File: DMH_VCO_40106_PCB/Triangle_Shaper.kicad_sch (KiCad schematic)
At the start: 15 parts, among them Q3 BC548, Q4 BC548, U3 TL072

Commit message: Added Cermet 3296W fp to trimpots
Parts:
- RV8: footprint (none) -> Potentiometer_THT:Potentiometer_Bourns_3296W_Vertical
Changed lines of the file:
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@@
 			)
 		)
-		(property "Footprint" ""
+		(property "Footprint" "Potentiometer_THT:Potentiometer_Bourns_3296W_Vertical"
 			(at 121.92 83.82 0)
 			(effects

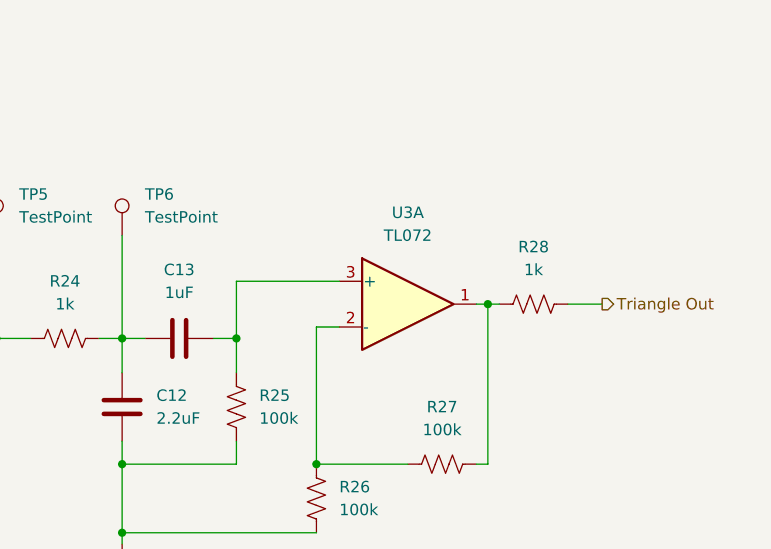
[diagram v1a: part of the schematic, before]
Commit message: Made U3 into TL074 instead of TL072
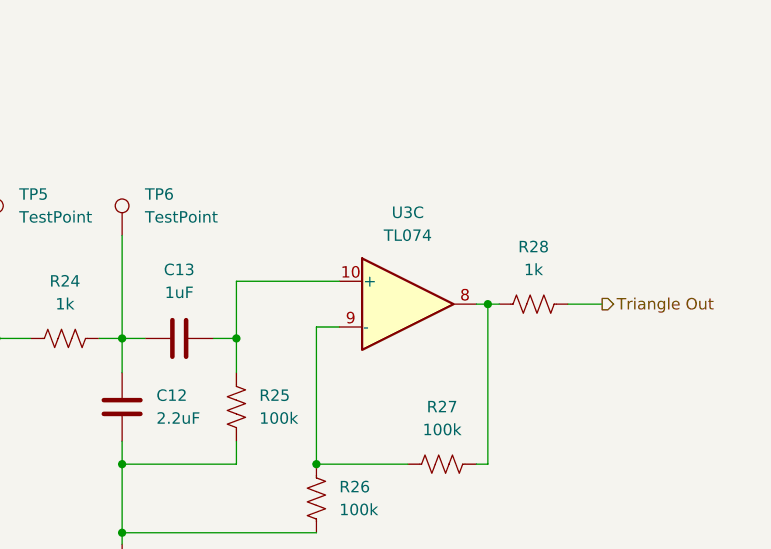
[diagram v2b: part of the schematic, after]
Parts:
- removed U3: TL072, symbol Amplifier_Operational:TL072
- added U3: TL074, symbol Amplifier_Operational:TL074
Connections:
- net at R26.1, R27.1: now also U3.9 (-)
- net at R27.2, R28.1: now also U3.8
- net at C13.2, R25.1: now also U3.10 (+)
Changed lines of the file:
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@@
+	)
+	(symbol
+		(lib_id "Amplifier_Operational:TL074")
+		(at 181.61 96.52 0)
+		(unit 3)
+		(exclude_from_sim no)
+		(in_bom yes)
+		(on_board yes)
+		(dnp no)
+		(fields_autoplaced yes)
+		(property "Reference" "U3"
+			(at 181.61 86.36 0)
+			(effects
+				(font
+					(size 1.27 1.27)
+				)
+			)
+		)
+		(property "Value" "TL074"
+			(at 181.61 88.9 0)
+			(effects
+				(font
+					(size 1.27 1.27)
+				)
+			)
+		)
+		(property "Footprint" ""
+			(at 180.34 93.98 0)
+			(effects
+				(font
+					(size 1.27 1.27)
+				)
+				(hide yes)
+			)
+		)
+		(property "Datasheet" "http://www.ti.com/lit/ds/symlink/tl071.pdf"
+			(at 182.88 91.44 0)
+			(effects
+				(font
+					(size 1.27 1.27)
+				)
+				(hide yes)
+			)
+		)
+		(property "Description" "Quad Low-Noise JFET-Input Operational Amplifiers, DIP-14/SOIC-14"
+			(at 181.61 96.52 0)
+			(effects
+				(font
+					(size 1.27 1.27)
+				)
+				(hide yes)
+			)
+		)
+		(pin "5"
+		)
+		(pin "1"
+		)
+		(pin "8"
+		)
+		(pin "13"
+		)
+		(pin "6"
+		)
+		(pin "14"
+		)
+		(pin "10"
+		)
+		(pin "9"
+		)
+		(pin "11"
+		)
+		(pin "3"
+		)
+		(pin "7"
+		)
+		(pin "12"
+		)
+		(pin "2"
+		)
+		(pin "4"
+		)
+		(instances
+			(project ""
+				(path "/fefed352-c100-4617-bbfb-c55e7427b122/0e77ed5b-450a-412c-a492-589f053c9c73"
+					(reference "U3")
+					(unit 3)
+				)
+			)
+		)
 	)
 	(symbol
@@
 					(unit 1)
 				)
-			)
-		)
-	)
-	(symbol
-		(lib_id "Amplifier_Operational:TL072")
-		(at 181.61 96.52 0)
-		(unit 1)
-		(exclude_from_sim no)
-		(in_bom yes)
-		(on_board yes)
-		(dnp no)
-		(fields_autoplaced yes)
-		(property "Reference" "U3"
-			(at 181.61 86.36 0)
-			(effects
-				(font
-					(size 1.27 1.27)
-				)
-			)
-		)
-		(property "Value" "TL072"
-			(at 181.61 88.9 0)
-			(effects
-				(font
-					(size 1.27 1.27)
-				)
-			)
-		)
-		(property "Footprint" ""
-			(at 181.61 96.52 0)
-			(effects
-				(font
-					(size 1.27 1.27)
-				)
-				(hide yes)
-			)
-		)
-		(property "Datasheet" "http://www.ti.com/lit/ds/symlink/tl071.pdf"
-			(at 181.61 96.52 0)
-			(effects
-				(font
-					(size 1.27 1.27)
-				)
-				(hide yes)
-			)
-		)
-		(property "Description" "Dual Low-Noise JFET-Input Operational Amplifiers, DIP-8/SOIC-8"
-			(at 181.61 96.52 0)
-			(effects
-				(font
-					(size 1.27 1.27)
-				)
-				(hide yes)
-			)
-		)
-		(pin "5"
-		)
-		(pin "1"
-		)
-		(pin "8"
-		)
-		(pin "7"
-		)
-		(pin "2"
-		)
-		(pin "4"
-		)
-		(pin "3"
-		)
-		(pin "6"
-		)
-		(instances
-			(project ""
-				(path "/fefed352-c100-4617-bbfb-c55e7427b122/0e77ed5b-450a-412c-a492-589f053c9c73"
-					(reference "U3")
-					(unit 1)
-				)

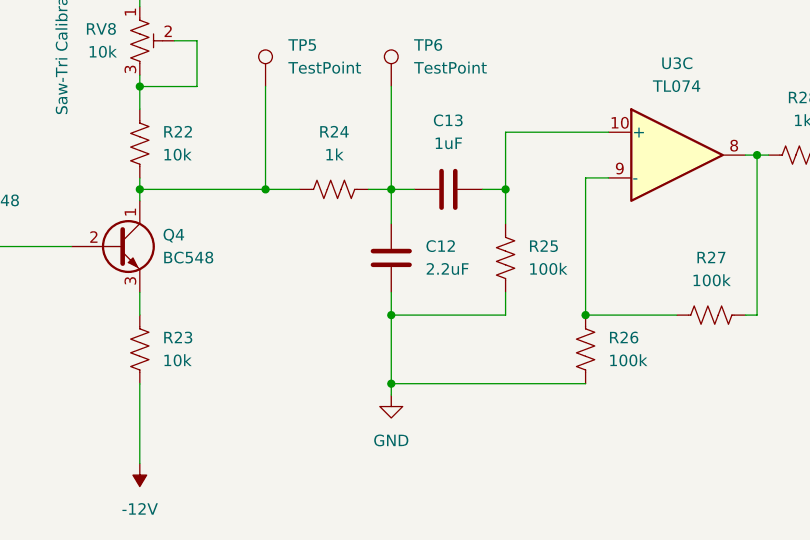
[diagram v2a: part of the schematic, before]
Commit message: Added not about 2.2uF cap
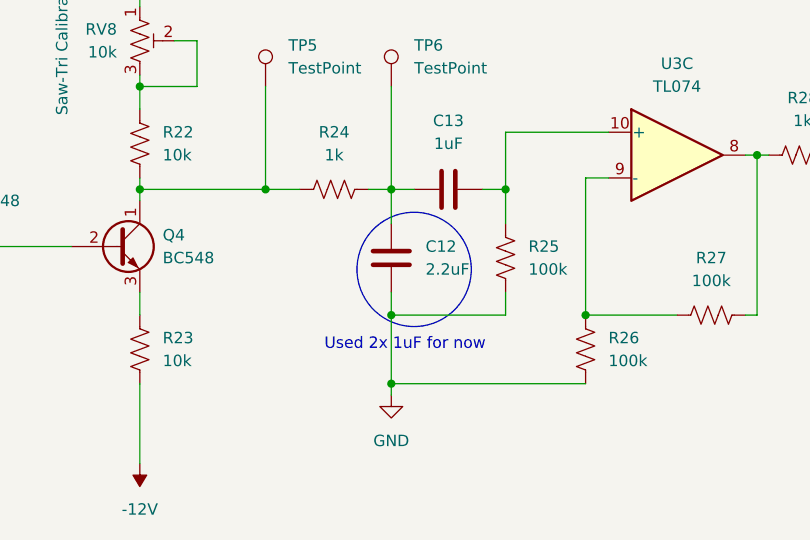
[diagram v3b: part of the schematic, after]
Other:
- note added: "Used 2x 1uF for now"
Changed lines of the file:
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@@
+		)
+	)
+	(circle
+		(center 152.4 109.22)
+		(radius 6.35)
+		(stroke
+			(width 0)
+			(type default)
+		)
+		(fill
+			(type none)
+		)
+	)
+	(text "Used 2x 1uF for now"
+		(exclude_from_sim no)
+		(at 151.384 117.602 0)
+		(effects
+			(font
+				(size 1.27 1.27)
+			)
 		)
 	)

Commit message: Corrected capacitor value
Should be 2.2nF, not 2.2uF
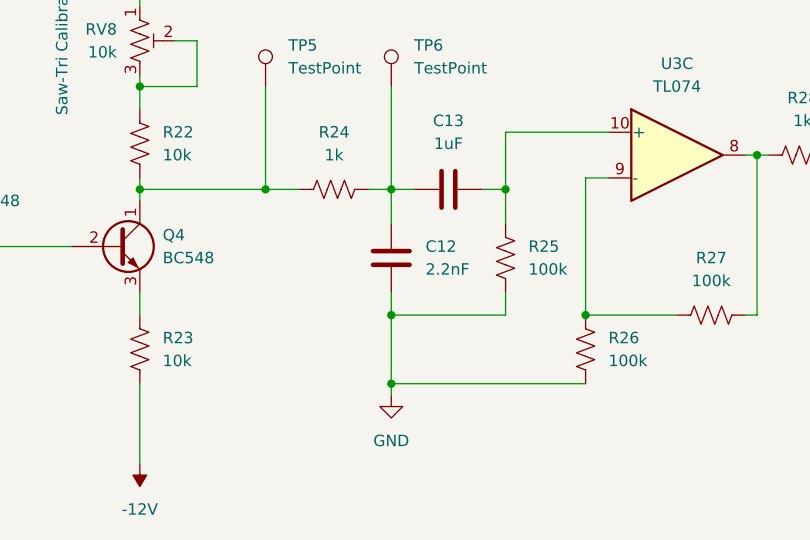
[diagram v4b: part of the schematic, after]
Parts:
- C12: value 2.2uF -> 2.2nF
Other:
- note removed: "Used 2x 1uF for now"
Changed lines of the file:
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@@
-		)
-	)
-	(circle
-		(center 152.4 109.22)
-		(radius 6.35)
-		(stroke
-			(width 0)
-			(type default)
-		)
-		(fill
-			(type none)
-		)
-	)
-	(text "Used 2x 1uF for now"
-		(exclude_from_sim no)
-		(at 151.384 117.602 0)
-		(effects
-			(font
-				(size 1.27 1.27)
-			)
 		)
 	)
@@
 			)
 		)
-		(property "Value" "2.2uF"
+		(property "Value" "2.2nF"
 			(at 153.67 109.2199 0)
 			(effects

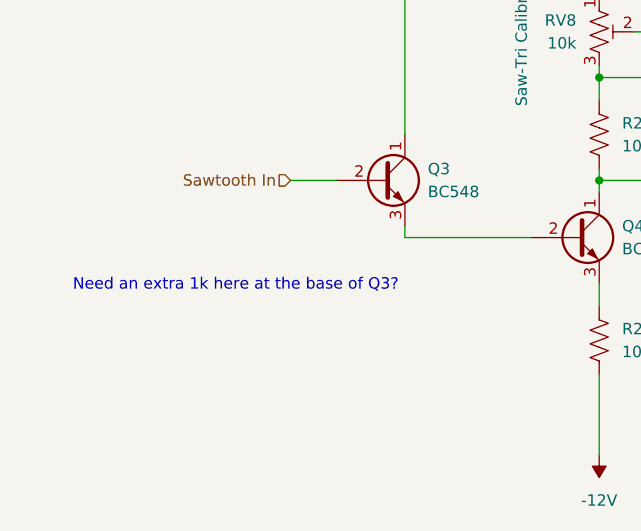
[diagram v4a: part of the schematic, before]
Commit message: Improved range of Coarse knob
... and allowed Centering knob to set C1=32,7Hz as root note with Coarse knob all the way CCW.
... and added 1kHz to Sine output.
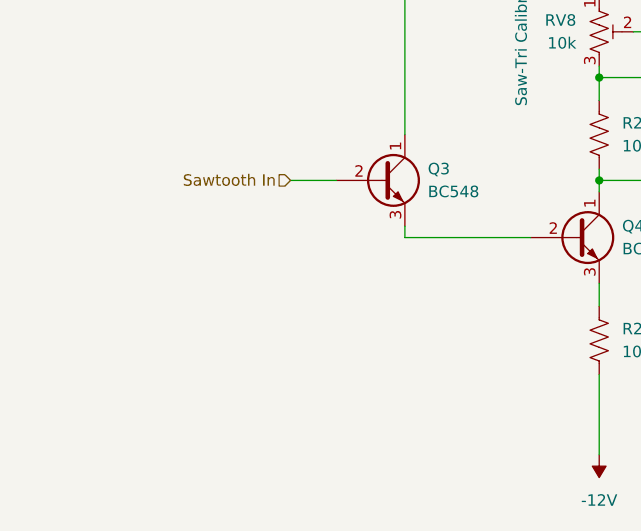
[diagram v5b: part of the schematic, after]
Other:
- note removed: "Need an extra 1k here at the base of Q3?"
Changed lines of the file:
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@@
-		)
-	)
-	(text "Need an extra 1k here at the base of Q3?"
-		(exclude_from_sim no)
-		(at 81.534 112.014 0)
-		(effects
-			(font
-				(size 1.27 1.27)
-			)
 		)
 	)

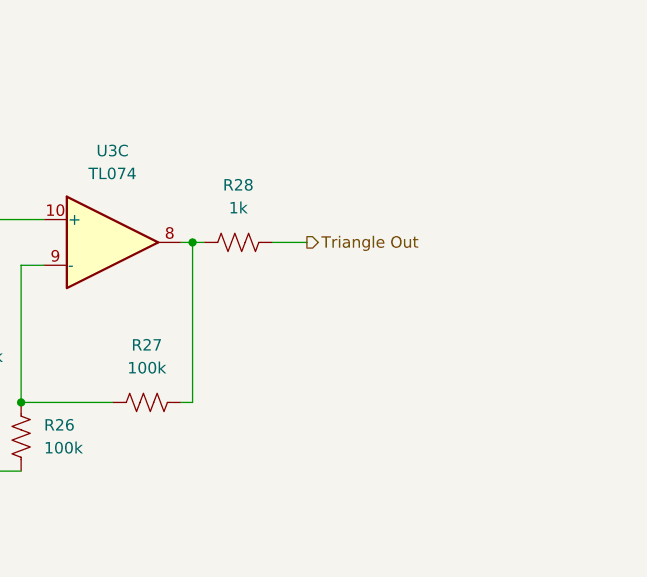
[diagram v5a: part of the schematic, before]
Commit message: Adjusted all output gains to 10Vpp
... and added buffer stages for Sawtooth Out and Triangle Out in order to avoid modifying Triangle and Sine wafeform characteristics when connecting Sawtooth Out and Triangle Out to other modules.
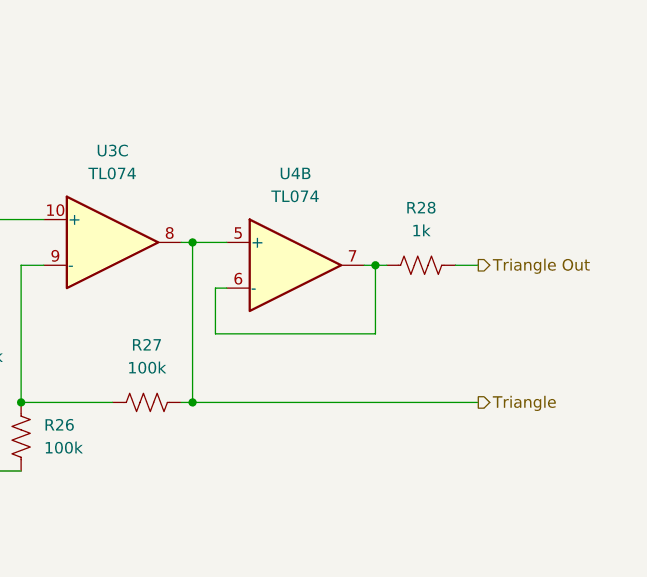
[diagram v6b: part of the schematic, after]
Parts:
- added U4: TL074, symbol Amplifier_Operational:TL074
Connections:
- net Triangle: now reaches R27.2, U3.8
- net Triangle: now also U4.5 (+); no longer R28.1
- new net: R28.1, U4.6 (-), U4.7
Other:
- moved on the sheet: R28
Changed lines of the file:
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@@
+	)
+	(junction
+		(at 210.82 99.06)
+		(diameter 0)
+		(color 0 0 0 0)
+	)
+	(junction
+		(at 121.92 100.33)
+		(diameter 0)
+		(color 0 0 0 0)
+	)
+	(junction
+		(at 121.92 72.39)
+		(diameter 0)
+		(color 0 0 0 0)
+	)
+	(junction
+		(at 190.5 114.3)
+		(diameter 0)
+		(color 0 0 0 0)
+	)
+	(junction
+		(at 162.56 100.33)
+		(diameter 0)
+		(color 0 0 0 0)
+	)
+	(junction
+		(at 149.86 114.3)
+		(diameter 0)
+		(color 0 0 0 0)
 	)
 	(junction
@@
 		(color 0 0 0 0)
 	)
-	(junction
-		(at 121.92 100.33)
-		(diameter 0)
-		(color 0 0 0 0)
-	)
-	(junction
-		(at 121.92 72.39)
-		(diameter 0)
-		(color 0 0 0 0)
-	)
-	(junction
-		(at 162.56 100.33)
-		(diameter 0)
-		(color 0 0 0 0)
-	)
-	(junction
-		(at 149.86 114.3)
-		(diameter 0)
-		(color 0 0 0 0)
-	)
 	(wire
 		(pts
@@
 	(wire
 		(pts
+			(xy 193.04 101.6) (xy 193.04 106.68)
+		)
+		(stroke
+			(width 0)
+			(type default)
+		)
+	)
+	(wire
+		(pts
 			(xy 162.56 93.98) (xy 173.99 93.98)
 		)
@@
 	(wire
 		(pts
-			(xy 190.5 96.52) (xy 190.5 114.3)
+			(xy 190.5 114.3) (xy 190.5 96.52)
 		)
 		(stroke
@@
 	(wire
 		(pts
-			(xy 189.23 96.52) (xy 190.5 96.52)
+			(xy 190.5 96.52) (xy 194.31 96.52)
+		)
+		(stroke
+			(width 0)
+			(type default)
+		)
+	)
+	(wire
+		(pts
+			(xy 193.04 106.68) (xy 210.82 106.68)
 		)
 		(stroke
@@
 	(wire
 		(pts
+			(xy 194.31 101.6) (xy 193.04 101.6)
+		)
+		(stroke
+			(width 0)
+			(type default)
+		)
+	)
+	(wire
+		(pts
 			(xy 121.92 88.9) (xy 121.92 91.44)
 		)
@@
 	(wire
 		(pts
+			(xy 210.82 106.68) (xy 210.82 99.06)
+		)
+		(stroke
+			(width 0)
+			(type default)
+		)
+	)
+	(wire
+		(pts
 			(xy 162.56 111.76) (xy 162.56 114.3)
 		)
@@
 	(wire
 		(pts
+			(xy 190.5 114.3) (xy 222.25 114.3)
+		)
+		(stroke
+			(width 0)
+			(type default)
+		)
+	)
+	(wire
+		(pts
 			(xy 135.89 100.33) (xy 139.7 100.33)
 		)
@@
 	(wire
 		(pts
-			(xy 190.5 96.52) (xy 191.77 96.52)
-		)
-		(stroke
-			(width 0)
-			(type default)
-		)
-	)
-	(wire
-		(pts
-			(xy 199.39 96.52) (xy 203.2 96.52)
+			(xy 190.5 96.52) (xy 189.23 96.52)
 		)
 		(stroke
@@
 	(wire
 		(pts
+			(xy 209.55 99.06) (xy 210.82 99.06)
+		)
+		(stroke
+			(width 0)
+			(type default)
+		)
+	)
+	(wire
+		(pts
 			(xy 100.33 72.39) (xy 121.92 72.39)
 		)
@@
 		(pts
 			(xy 149.86 114.3) (xy 149.86 121.92)
+		)
+		(stroke
+			(width 0)
+			(type default)
+		)
+	)
+	(wire
+		(pts
+			(xy 219.71 99.06) (xy 222.25 99.06)
+		)
+		(stroke
+			(width 0)
+			(type default)
+		)
+	)
+	(wire
+		(pts
+			(xy 210.82 99.06) (xy 212.09 99.06)
 		)
 		(stroke
@@
 	(hierarchical_label "Triangle Out"
 		(shape output)
-		(at 203.2 96.52 0)
+		(at 222.25 99.06 0)
 		(fields_autoplaced yes)
 		(effects
@@
 			)
 			(justify right)
+		)
+	)
+	(hierarchical_label "Triangle"
+		(shape output)
+		(at 222.25 114.3 0)
+		(fields_autoplaced yes)
+		(effects
+			(font
+				(size 1.27 1.27)
+			)
+			(justify left)
 		)
 	)
@@
 	(symbol
 		(lib_id "Device:R_US")
-		(at 195.58 96.52 90)
+		(at 215.9 99.06 90)
 		(unit 1)
 		(exclude_from_sim no)
@@
 		(fields_autoplaced yes)
 		(property "Reference" "R28"
-			(at 195.58 90.17 90)
+			(at 215.9 92.71 90)
 			(effects
 				(font
@@
 		)
 		(property "Value" "1k"
-			(at 195.58 92.71 90)
+			(at 215.9 95.25 90)
 			(effects
 				(font
@@
 		)
 		(property "Footprint" "Resistor_THT:R_Axial_DIN0204_L3.6mm_D1.6mm_P5.08mm_Horizontal"
-			(at 195.834 95.504 90)
+			(at 216.154 98.044 90)
 			(effects
 				(font
@@
 		)
 		(property "Datasheet" "~"
-			(at 195.58 96.52 0)
+			(at 215.9 99.06 0)
 			(effects
 				(font
@@
 		)
 		(property "Description" "Resistor, US symbol"
-			(at 195.58 96.52 0)
+			(at 215.9 99.06 0)
 			(effects
 				(font
@@
 				)
 			)
+		)
+	)
+	(symbol
+		(lib_id "Amplifier_Operational:TL074")
+		(at 201.93 99.06 0)
+		(unit 2)
+		(exclude_from_sim no)
+		(in_bom yes)
+		(on_board yes)
+		(dnp no)
+		(fields_autoplaced yes)
+		(property "Reference" "U4"
+			(at 201.93 88.9 0)
+			(effects
+				(font
+					(size 1.27 1.27)
+				)
+			)
+		)
+		(property "Value" "TL074"
+			(at 201.93 91.44 0)
+			(effects
+				(font
+					(size 1.27 1.27)
+				)
+			)
+		)
+		(property "Footprint" ""
+			(at 200.66 96.52 0)
+			(effects
+				(font
+					(size 1.27 1.27)
+				)
+				(hide yes)
+			)
+		)
+		(property "Datasheet" "http://www.ti.com/lit/ds/symlink/tl071.pdf"
+			(at 203.2 93.98 0)
+			(effects
+				(font
+					(size 1.27 1.27)
+				)
+				(hide yes)
+			)
+		)
+		(property "Description" "Quad Low-Noise JFET-Input Operational Amplifiers, DIP-14/SOIC-14"
+			(at 201.93 99.06 0)
+			(effects
+				(font
+					(size 1.27 1.27)
+				)
+				(hide yes)
+			)
+		)
+		(pin "3"
+		)
+		(pin "2"
+		)
+		(pin "12"
+		)
+		(pin "13"
+		)
+		(pin "11"
+		)
+		(pin "10"
+		)
+		(pin "8"
+		)
+		(pin "14"
+		)
+		(pin "6"
+		)
+		(pin "9"
+		)
+		(pin "1"
+		)
+		(pin "4"
+		)
+		(pin "5"
+		)
+		(pin "7"
+		)
+		(instances
+			(project ""
+				(path "/fefed352-c100-4617-bbfb-c55e7427b122/0e77ed5b-450a-412c-a492-589f053c9c73"
+					(reference "U4")
+					(unit 2)
+				)
+			)

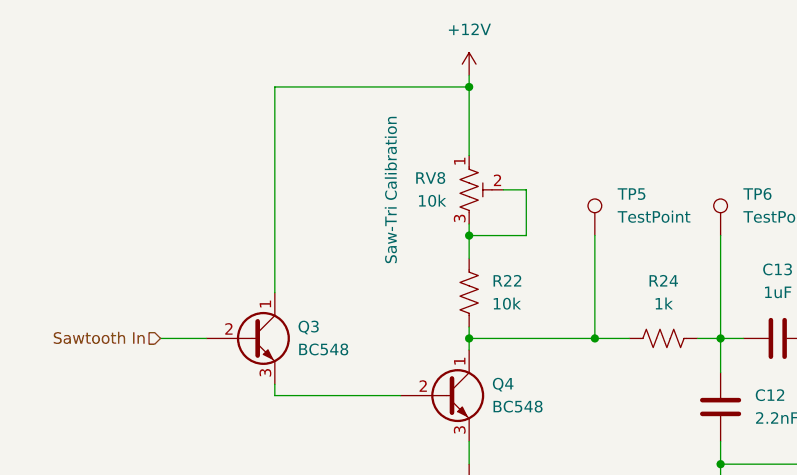
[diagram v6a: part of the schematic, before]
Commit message: Updated Tuner
- Changed uC to ATtiny4313
- Added LEDs
- Created "function" field and updated all jacks, switches and pots
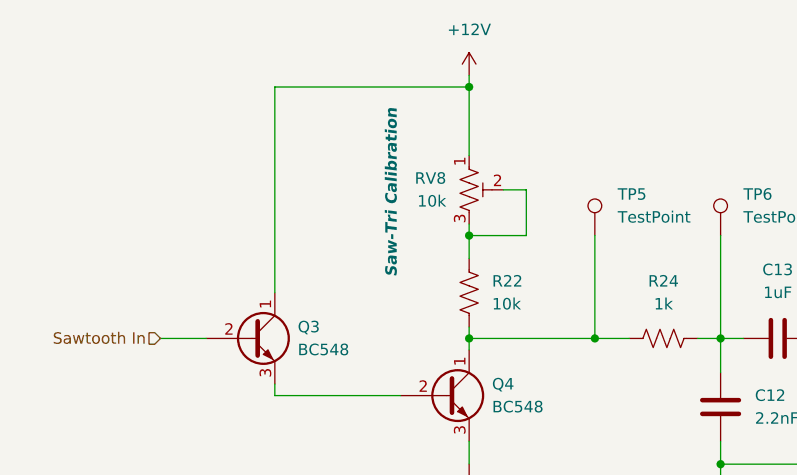
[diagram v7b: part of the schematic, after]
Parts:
- RV8: Function (none) -> Saw-Tri Calibration
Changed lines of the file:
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@@
 			)
 		)
-		(property "Description" "Saw-Tri Calibration"
+		(property "Description" ""
 			(at 113.284 83.82 90)
 			(effects
@@
 					(size 1.27 1.27)
 				)
+				(hide yes)
 			)
+		)
+		(property "Function" "Saw-Tri Calibration"
+			(at 113.284 84.074 90)
+			(effects
+				(font
+					(size 1.27 1.27)
+					(bold yes)
+					(italic yes)
+				)
+			)

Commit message: Fixed trimpot fp linking
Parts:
- U3: footprint (none) -> Package_DIP:DIP-14_W7.62mm_Socket
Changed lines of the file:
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@@
 			)
 		)
-		(property "Footprint" ""
+		(property "Footprint" "Package_DIP:DIP-14_W7.62mm_Socket"
 			(at 180.34 93.98 0)
 			(effects
